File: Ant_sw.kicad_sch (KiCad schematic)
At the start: 0 parts

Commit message: vswr and antenna switch schematic added
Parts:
- added C5, C51, C52 (x6), C6 (x9): 10n, Capacitor_SMD:C_0805_2012Metric_Pad1.18x1.45mm_HandSolder, symbol Device:C_Small
- added C51 (x2): 100n, Capacitor_SMD:C_0805_2012Metric_Pad1.18x1.45mm_HandSolder, symbol Device:C_Small
- added D1 (x5): D_Small, symbol Device:D_Small
- added D4 (x5): LED_Small, symbol Device:LED_Small
- added FB2 (x5): FerriteBead_Small, symbol Device:FerriteBead_Small
- added J1 (x5): Conn_Coaxial, symbol Connector:Conn_Coaxial
- added K2 (x5): G2R-1-E DC12, RELAY_G2R-1-E AC12:RELAY_G2R-1-E AC12, symbol RELAY_G2R-1-E AC12:G2R-1-E_DC12
- added Q1: 2N7002, Package_TO_SOT_SMD:SOT-23, symbol Transistor_FET:2N7002
- added R2 (x5): 2k7, Resistor_SMD:R_0805_2012Metric_Pad1.20x1.40mm_HandSolder, symbol Device:R_Small
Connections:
- new net: C51.1, C52.1, C6.1, C6.1, C6.1, C6.1, C6.1, D1.1 (K), D1.1 (K), D1.1 (K), D1.1 (K), D1.1 (K), D4.2 (A), D4.2 (A), D4.2 (A), D4.2 (A), D4.2 (A), FB2.2, K2.1, K2.1, K2.1, K2.1, K2.1
- new net: C6.1, D1.2 (A), FB2.2, K2.8, R2.1 (x3)
- new net: C5.1, C6.1, D1.2 (A), D1.2 (A), K2.8, K2.8, Q1.3 (D), R2.1, R2.1
- new net: D4.1 (K), R2.2 (x5)
- new net: C51.1, FB2.2, Q1.1 (G)
- new net: J1.1 (In), K2.4, K2.5 (x4)
- new net: K2.2, K2.7 (x3)
- new net: K2.3, K2.3, K2.3, K2.3, K2.6, K2.6, K2.6, K2.6
- new net: K2.2, K2.2, K2.7, K2.7
- new net: J1.1 (In), K2.3, K2.6
- new net +12V_R: C51.1, C52.1, FB2.1
- new net ANT1: C52.1, FB2.1
- new net ANT2: C52.1, FB2.1
- new net ANT3: C52.1, FB2.1
- new net ATU_OUT: K2.4, K2.5
- new net GND: C5.2, C51.2, C51.2, C51.2, C52.2, C52.2, C52.2, C52.2, C52.2, C52.2, C6.2, C6.2, C6.2, C6.2, C6.2, C6.2, C6.2, C6.2, C6.2, J1.2 (Ext), J1.2 (Ext), J1.2 (Ext), J1.2 (Ext), J1.2 (Ext), Q1.2 (S)
- new net T/R_PTT: C52.1, FB2.1
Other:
- note added: "ANT1"
- note added: "ANT2"
- note added: "ANT3"
- note added: "From TX Ant"
- note added: "To Ant_In"
- note added: "Vérifier le câblage du relais Ant1 qui me semble merdeux sur le schéma d'origine"

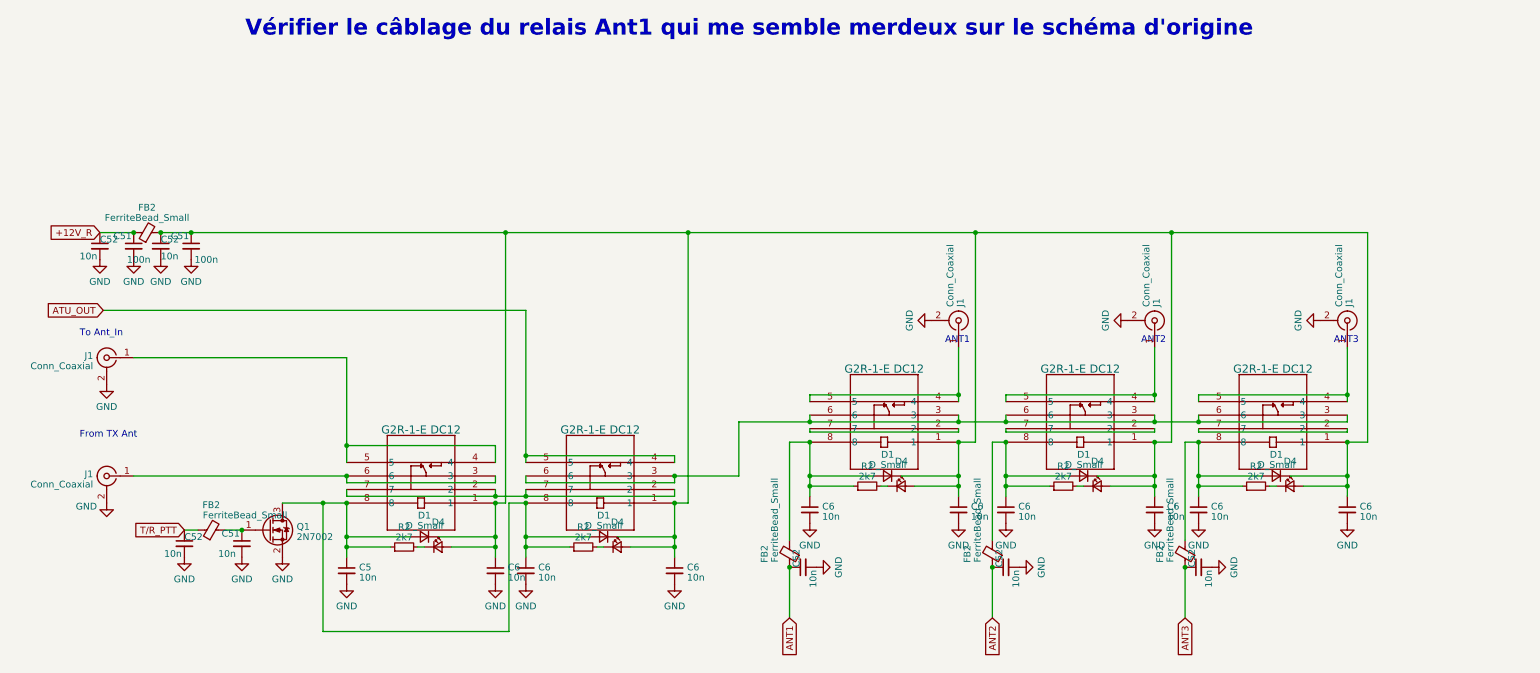
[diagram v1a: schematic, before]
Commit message: schematic fully captured
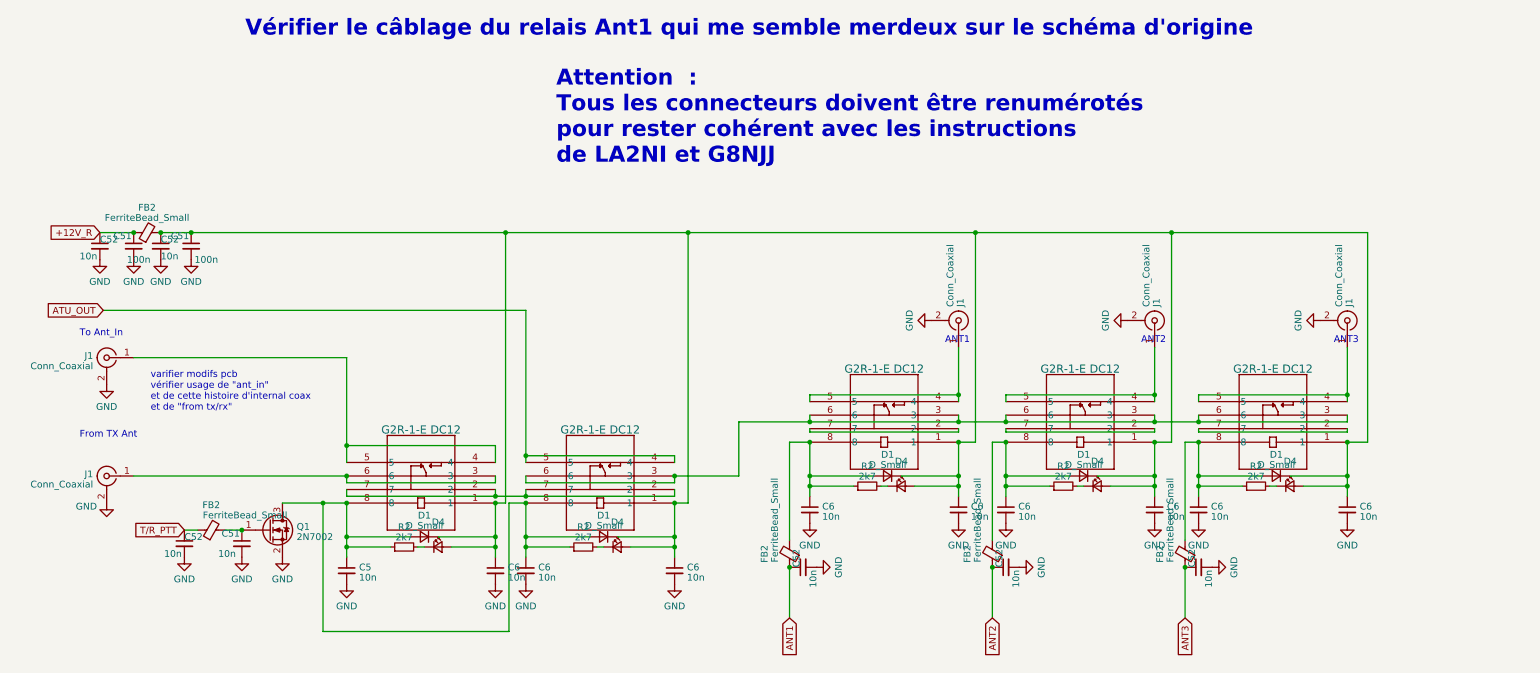
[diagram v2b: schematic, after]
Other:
- note added: "Attention : Tous les connecteurs doivent être renumérotés pour rester cohérent avec les instructions de LA2NI et G8NJJ"
- note added: "varifier modifs pcb vérifier usage de "ant_in" et de cette histoire d'internal coax et de "from tx/rx""

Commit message: component-footprint association
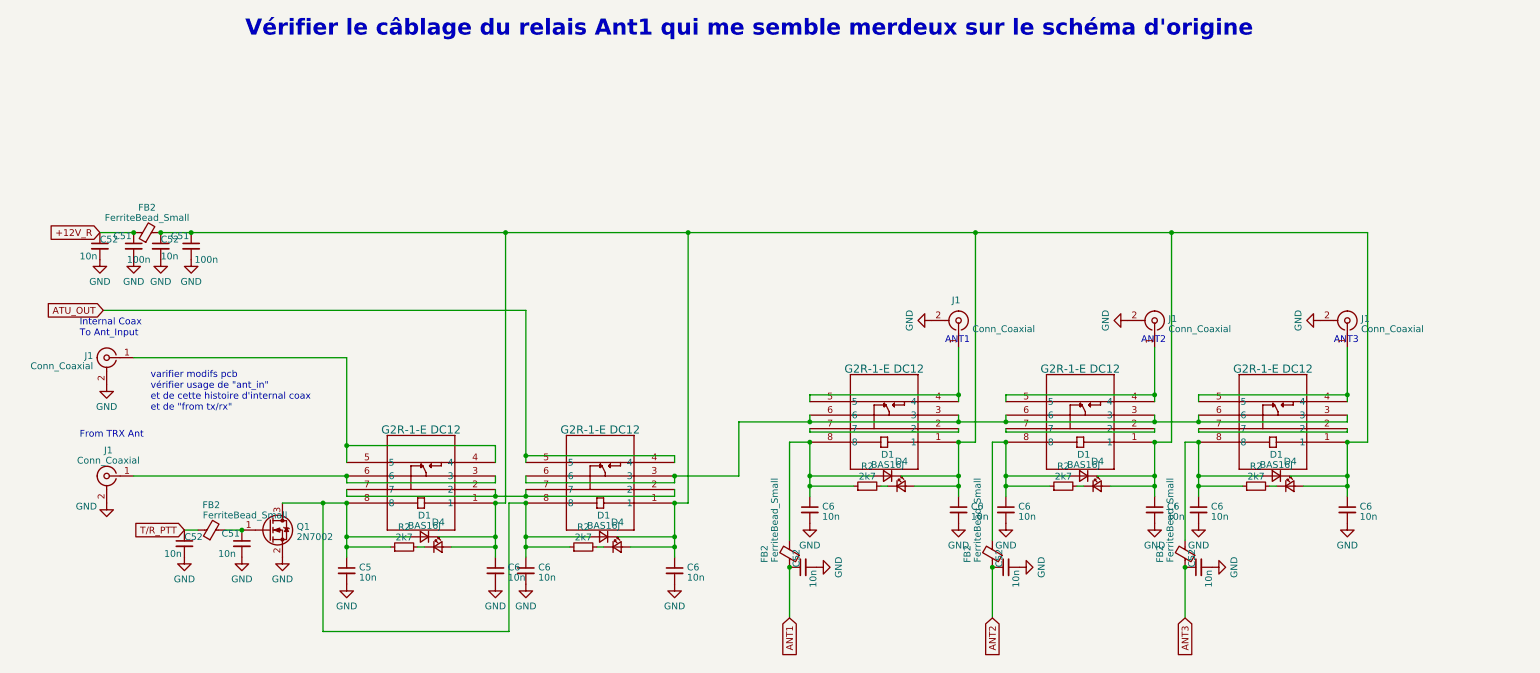
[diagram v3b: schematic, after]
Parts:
- D1: value D_Small -> BAS16J; footprint (none) -> Diode_SMD:D_SOD-323_HandSoldering
- D4: footprint (none) -> LED_SMD:LED_1206_3216Metric_Pad1.42x1.75mm_HandSolder
- FB2: footprint (none) -> Inductor_SMD:L_0805_2012Metric_Pad1.15x1.40mm_HandSolder
- FB2: footprint (none) -> Inductor_SMD:L_2512_6332Metric_Pad1.52x3.35mm_HandSolder
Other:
- note added: "From TRX Ant"
- note added: "Internal Coax To Ant_Input"
- note removed: "Attention : Tous les connecteurs doivent être renumérotés pour rester cohérent avec les instructions de LA2NI et G8NJJ"
- note removed: "From TX Ant"
- note removed: "To Ant_In"
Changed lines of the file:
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@@
     (stroke (width 0) (type default))
-  )
-  (text "Attention  : \nTous les connecteurs doivent être renumérotés\npour rester cohérent avec les instructions\nde LA2NI et G8NJJ"
-    (at 108.585 66.04 0)
-    (effects (font (size 3 3) (thickness 0.6) bold (color 255 38 42 1)) (justify left bottom))
   )
   (text "ANT2\n" (at 218.44 99.695 0)
@@
     (effects (font (size 3 3) (thickness 0.6) bold) (justify left bottom))
   )
-  (text "To Ant_In" (at 19.05 98.425 0)
+  (text "Internal Coax\nTo Ant_Input" (at 19.05 98.425 0)
     (effects (font (size 1.27 1.27)) (justify left bottom))
   )
@@
     (effects (font (size 1.27 1.27)) (justify left bottom))
   )
-  (text "From TX Ant" (at 19.05 117.475 0)
+  (text "From TRX Ant" (at 19.05 117.475 0)
     (effects (font (size 1.27 1.27)) (justify left bottom))
   )
@@
       (effects (font (size 1.27 1.27)))
     )
-    (property "Value" "D_Small" (at 207.645 122.3551 0)
-      (effects (font (size 1.27 1.27)))
-    )
-    (property "Footprint" "" (at 207.645 124.46 90)
+    (property "Value" "BAS16J" (at 207.645 122.3551 0)
+      (effects (font (size 1.27 1.27)))
+    )
+    (property "Footprint" "Diode_SMD:D_SOD-323_HandSoldering" (at 207.645 124.46 90)
       (effects (font (size 1.27 1.27)) hide)
     )
@@
       (effects (font (size 1.27 1.27)))
     )
-    (property "Footprint" "" (at 228.473 139.065 90)
+    (property "Footprint" "Inductor_SMD:L_0805_2012Metric_Pad1.15x1.40mm_HandSolder" (at 228.473 139.065 90)
       (effects (font (size 1.27 1.27)) hide)
     )
@@
       (effects (font (size 1.27 1.27)))
     )
-    (property "Value" "D_Small" (at 170.815 122.3551 0)
-      (effects (font (size 1.27 1.27)))
-    )
-    (property "Footprint" "" (at 170.815 124.46 90)
+    (property "Value" "BAS16J" (at 170.815 122.3551 0)
+      (effects (font (size 1.27 1.27)))
+    )
+    (property "Footprint" "Diode_SMD:D_SOD-323_HandSoldering" (at 170.815 124.46 90)
       (effects (font (size 1.27 1.27)) hide)
     )
@@
       (effects (font (size 1.27 1.27)))
     )
-    (property "Footprint" "" (at 154.178 139.065 90)
+    (property "Footprint" "Inductor_SMD:L_0805_2012Metric_Pad1.15x1.40mm_HandSolder" (at 154.178 139.065 90)
       (effects (font (size 1.27 1.27)) hide)
     )
@@
       (effects (font (size 1.27 1.27)) hide)
     )
-    (property "Footprint" "" (at 86.36 137.795 90)
+    (property "Footprint" "LED_SMD:LED_1206_3216Metric_Pad1.42x1.75mm_HandSolder" (at 86.36 137.795 90)
       (effects (font (size 1.27 1.27)) hide)
     )
@@
       (effects (font (size 1.27 1.27)))
     )
-    (property "Value" "D_Small" (at 83.82 133.7851 0)
-      (effects (font (size 1.27 1.27)))
-    )
-    (property "Footprint" "" (at 83.82 135.89 90)
+    (property "Value" "BAS16J" (at 83.82 133.7851 0)
+      (effects (font (size 1.27 1.27)))
+    )
+    (property "Footprint" "Diode_SMD:D_SOD-323_HandSoldering" (at 83.82 135.89 90)
       (effects (font (size 1.27 1.27)) hide)
     )
@@
       (effects (font (size 1.27 1.27)) hide)
     )
-    (property "Footprint" "" (at 210.185 126.365 90)
+    (property "Footprint" "LED_SMD:LED_1206_3216Metric_Pad1.42x1.75mm_HandSolder" (at 210.185 126.365 90)
       (effects (font (size 1.27 1.27)) hide)
     )
@@
       (effects (font (size 1.27 1.27)))
     )
-    (property "Footprint" "" (at 31.75 80.518 90)
+    (property "Footprint" "Inductor_SMD:L_2512_6332Metric_Pad1.52x3.35mm_HandSolder" (at 31.75 80.518 90)
       (effects (font (size 1.27 1.27)) hide)
     )
@@
       (effects (font (size 1.27 1.27)))
     )
-    (property "Value" "D_Small" (at 117.475 133.7851 0)
-      (effects (font (size 1.27 1.27)))
-    )
-    (property "Footprint" "" (at 117.475 135.89 90)
+    (property "Value" "BAS16J" (at 117.475 133.7851 0)
+      (effects (font (size 1.27 1.27)))
+    )
+    (property "Footprint" "Diode_SMD:D_SOD-323_HandSoldering" (at 117.475 135.89 90)
       (effects (font (size 1.27 1.27)) hide)
     )
@@
       (effects (font (size 1.27 1.27)))
     )
-    (property "Footprint" "" (at 192.278 139.065 90)
+    (property "Footprint" "Inductor_SMD:L_0805_2012Metric_Pad1.15x1.40mm_HandSolder" (at 192.278 139.065 90)
       (effects (font (size 1.27 1.27)) hide)
     )
@@
       (effects (font (size 1.27 1.27)) hide)
     )
-    (property "Footprint" "" (at 173.355 126.365 90)
+    (property "Footprint" "LED_SMD:LED_1206_3216Metric_Pad1.42x1.75mm_HandSolder" (at 173.355 126.365 90)
       (effects (font (size 1.27 1.27)) hide)
     )
@@
   (symbol (lib_id "Connector:Conn_Coaxial") (at 24.13 124.46 0) (mirror y) (unit 1)
     (in_bom yes) (on_board yes) (dnp no) (fields_autoplaced)
-    (property "Reference" "J1" (at 21.5899 124.1095 0)
-      (effects (font (size 1.27 1.27)) (justify left))
-    )
-    (property "Value" "Conn_Coaxial" (at 21.5899 126.0305 0)
-      (effects (font (size 1.27 1.27)) (justify left))
+    (property "Reference" "J1" (at 24.4474 119.6235 0)
+      (effects (font (size 1.27 1.27)))
+    )
+    (property "Value" "Conn_Coaxial" (at 24.4474 121.5445 0)
+      (effects (font (size 1.27 1.27)))
     )
     (property "Footprint" "" (at 24.13 124.46 0)
@@
         )
         (path "/4d56c8f7-829b-457e-80cb-74e9f55628bb/70dfd9f7-6ecd-43f8-82c4-d1b5f4fc6a24"
-          (reference "J14") (unit 1)
+          (reference "J10") (unit 1)
         )
       )
@@
   (symbol (lib_id "Connector:Conn_Coaxial") (at 220.98 95.25 270) (mirror x) (unit 1)
     (in_bom yes) (on_board yes) (dnp no) (fields_autoplaced)
-    (property "Reference" "J1" (at 221.3305 92.7099 0)
-      (effects (font (size 1.27 1.27)) (justify left))
-    )
-    (property "Value" "Conn_Coaxial" (at 219.4095 92.7099 0)
+    (property "Reference" "J1" (at 223.5686 94.9237 90)
+      (effects (font (size 1.27 1.27)) (justify left))
+    )
+    (property "Value" "Conn_Coaxial" (at 223.5686 96.8447 90)
       (effects (font (size 1.27 1.27)) (justify left))
     )
@@
         )
         (path "/4d56c8f7-829b-457e-80cb-74e9f55628bb/70dfd9f7-6ecd-43f8-82c4-d1b5f4fc6a24"
-          (reference "J16") (unit 1)
+          (reference "J8") (unit 1)
         )
       )
@@
   )
   (symbol (lib_id "Connector:Conn_Coaxial") (at 184.15 95.25 270) (mirror x) (unit 1)
-    (in_bom yes) (on_board yes) (dnp no) (fields_autoplaced)
-    (property "Reference" "J1" (at 184.5005 92.7099 0)
-      (effects (font (size 1.27 1.27)) (justify left))
-    )
-    (property "Value" "Conn_Coaxial" (at 182.5795 92.7099 0)
+    (in_bom yes) (on_board yes) (dnp no)
+    (property "Reference" "J1" (at 182.88 91.44 90)
+      (effects (font (size 1.27 1.27)) (justify left))
+    )
+    (property "Value" "Conn_Coaxial" (at 186.7386 96.8447 90)
       (effects (font (size 1.27 1.27)) (justify left))
     )
@@
         )
         (path "/4d56c8f7-829b-457e-80cb-74e9f55628bb/70dfd9f7-6ecd-43f8-82c4-d1b5f4fc6a24"
-          (reference "J15") (unit 1)
+          (reference "J7") (unit 1)
         )
       )
@@
       (effects (font (size 1.27 1.27)))
     )
-    (property "Value" "D_Small" (at 243.84 122.3551 0)
-      (effects (font (size 1.27 1.27)))
-    )
-    (property "Footprint" "" (at 243.84 124.46 90)
+    (property "Value" "BAS16J" (at 243.84 122.3551 0)
+      (effects (font (size 1.27 1.27)))
+    )
+    (property "Footprint" "Diode_SMD:D_SOD-323_HandSoldering" (at 243.84 124.46 90)
       (effects (font (size 1.27 1.27)) hide)
     )
@@
       (effects (font (size 1.27 1.27)) hide)
     )
-    (property "Footprint" "" (at 246.38 126.365 90)
+    (property "Footprint" "LED_SMD:LED_1206_3216Metric_Pad1.42x1.75mm_HandSolder" (at 246.38 126.365 90)
       (effects (font (size 1.27 1.27)) hide)
     )
@@
       (effects (font (size 1.27 1.27)) hide)
     )
-    (property "Footprint" "" (at 120.015 137.795 90)
+    (property "Footprint" "LED_SMD:LED_1206_3216Metric_Pad1.42x1.75mm_HandSolder" (at 120.015 137.795 90)
       (effects (font (size 1.27 1.27)) hide)
     )
@@
       (effects (font (size 1.27 1.27)))
     )
-    (property "Footprint" "" (at 43.815 136.398 90)
+    (property "Footprint" "Inductor_SMD:L_2512_6332Metric_Pad1.52x3.35mm_HandSolder" (at 43.815 136.398 90)
       (effects (font (size 1.27 1.27)) hide)
     )
@@
   (symbol (lib_id "Connector:Conn_Coaxial") (at 257.175 95.25 270) (mirror x) (unit 1)
     (in_bom yes) (on_board yes) (dnp no) (fields_autoplaced)
-    (property "Reference" "J1" (at 257.5255 92.7099 0)
-      (effects (font (size 1.27 1.27)) (justify left))
-    )
-    (property "Value" "Conn_Coaxial" (at 255.6045 92.7099 0)
+    (property "Reference" "J1" (at 259.7636 94.9237 90)
+      (effects (font (size 1.27 1.27)) (justify left))
+    )
+    (property "Value" "Conn_Coaxial" (at 259.7636 96.8447 90)
       (effects (font (size 1.27 1.27)) (justify left))
     )
@@
         )
         (path "/4d56c8f7-829b-457e-80cb-74e9f55628bb/70dfd9f7-6ecd-43f8-82c4-d1b5f4fc6a24"
-          (reference "J17") (unit 1)
-        )
-      )
+          (reference "J9") (unit 1)
+        )
+      )

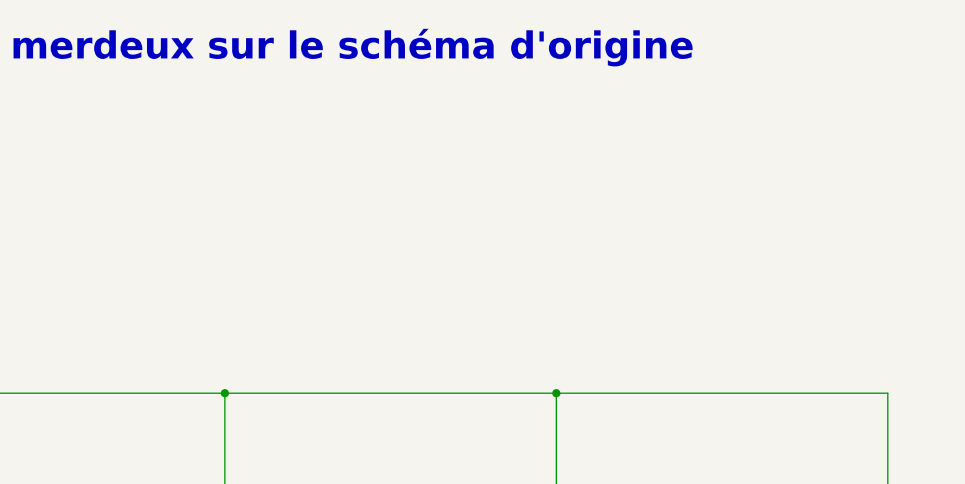
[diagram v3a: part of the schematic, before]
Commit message: all component sourced, all 3D object configured
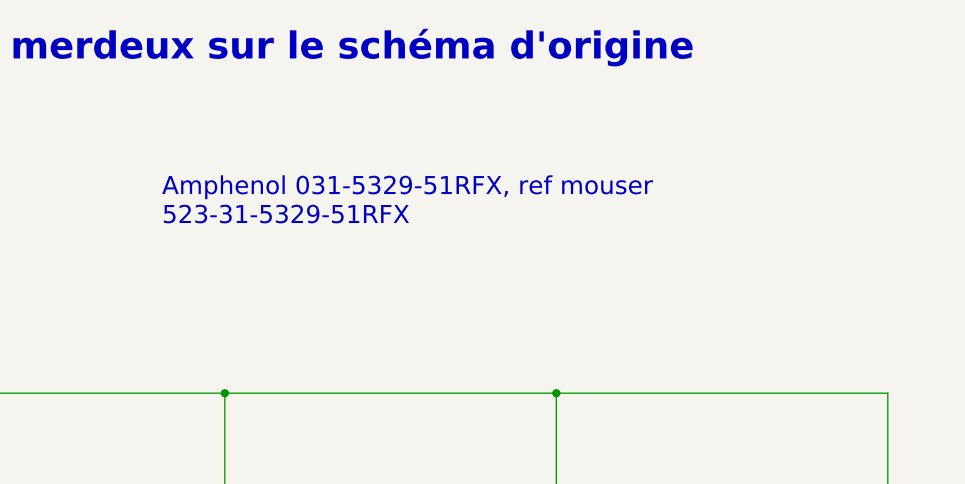
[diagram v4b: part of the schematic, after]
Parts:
- J1: footprint (none) -> BNC_Amphenol_031-5329-51RFX:BNC_Amphenol_031532951RFX
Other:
- note added: "Amphenol 031-5329-51RFX, ref mouser 523-31-5329-51RFX"
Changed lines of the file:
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@@
     (effects (font (size 1.27 1.27)) (justify left bottom))
+  )
+  (text "\nAmphenol 031-5329-51RFX, ref mouser \n523-31-5329-51RFX"
+    (at 180.34 60.325 0)
+    (effects (font (size 2 2)) (justify left bottom))
   )
   (text "ANT3\n" (at 254.635 99.695 0)
@@
       (effects (font (size 1.27 1.27)) (justify left))
     )
-    (property "Footprint" "" (at 24.13 102.235 0)
+    (property "Footprint" "BNC_Amphenol_031-5329-51RFX:BNC_Amphenol_031532951RFX" (at 24.13 102.235 0)
       (effects (font (size 1.27 1.27)) hide)
     )
@@
       (effects (font (size 1.27 1.27)))
     )
-    (property "Footprint" "" (at 24.13 124.46 0)
+    (property "Footprint" "BNC_Amphenol_031-5329-51RFX:BNC_Amphenol_031532951RFX" (at 24.13 124.46 0)
       (effects (font (size 1.27 1.27)) hide)
     )
@@
       (effects (font (size 1.27 1.27)) (justify left))
     )
-    (property "Footprint" "" (at 220.98 95.25 0)
+    (property "Footprint" "BNC_Amphenol_031-5329-51RFX:BNC_Amphenol_031532951RFX" (at 220.98 95.25 0)
       (effects (font (size 1.27 1.27)) hide)
     )
@@
       (effects (font (size 1.27 1.27)) (justify left))
     )
-    (property "Footprint" "" (at 184.15 95.25 0)
+    (property "Footprint" "BNC_Amphenol_031-5329-51RFX:BNC_Amphenol_031532951RFX" (at 184.15 95.25 0)
       (effects (font (size 1.27 1.27)) hide)
     )
@@
       (effects (font (size 1.27 1.27)) (justify left))
     )
-    (property "Footprint" "" (at 257.175 95.25 0)
-      (effects (font (size 1.27 1.27)) hide)
-    )
+    (property "Footprint" "BNC_Amphenol_031-5329-51RFX:BNC_Amphenol_031532951RFX" (at 257.175 95.25 0)
+      (effects (font (size 1.27 1.27)) hide)
+    )
